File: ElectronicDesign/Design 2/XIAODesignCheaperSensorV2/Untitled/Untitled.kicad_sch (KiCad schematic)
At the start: 22 parts, among them U1 XIAO-ESP32-C3-SMD, U2 MPR121QR2, U3 QMI8658A_C3021082, U6 S2B-PH-K-S

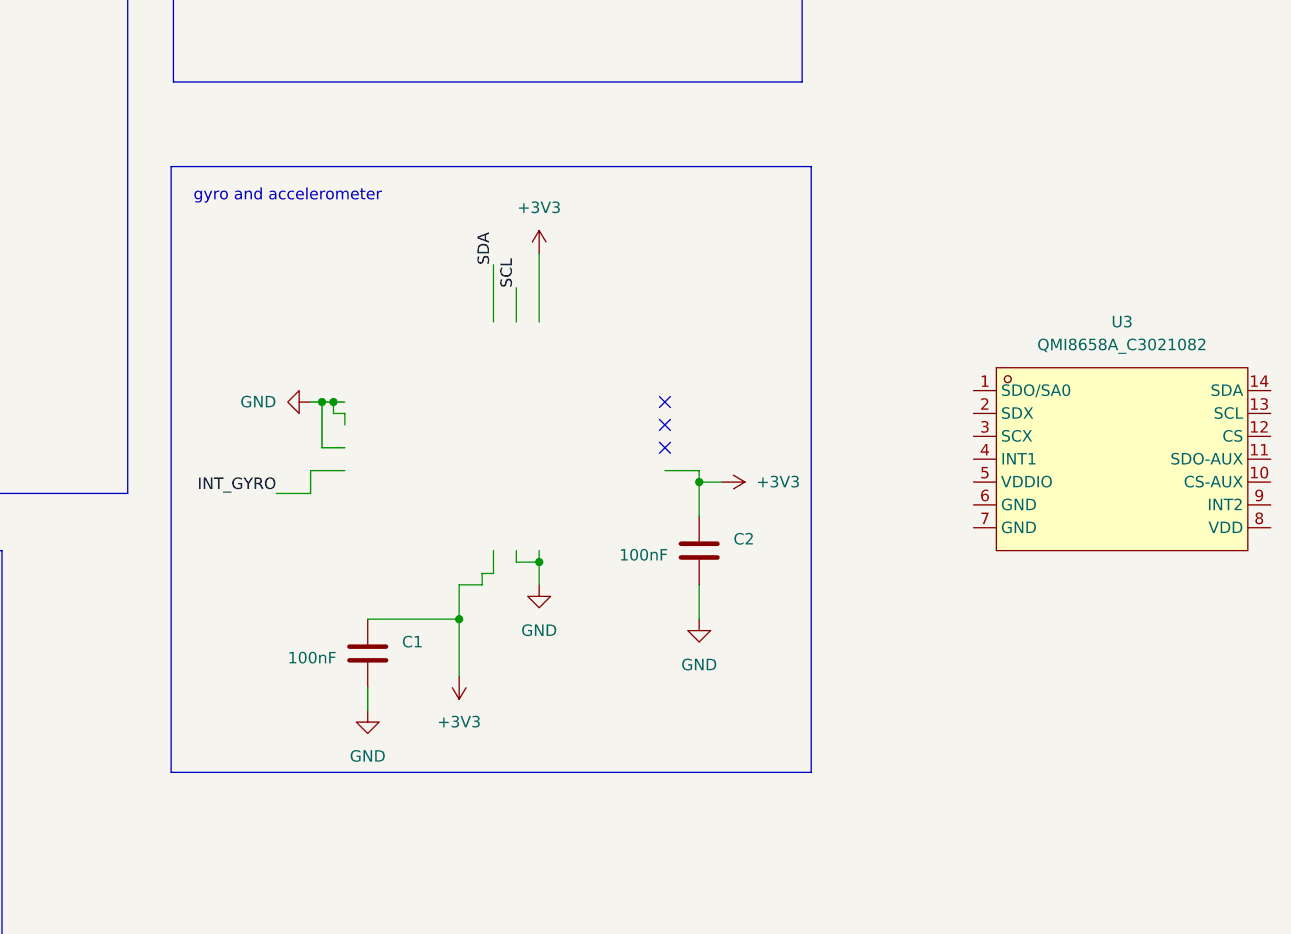
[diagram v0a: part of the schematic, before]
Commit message: Updated schematic with new component
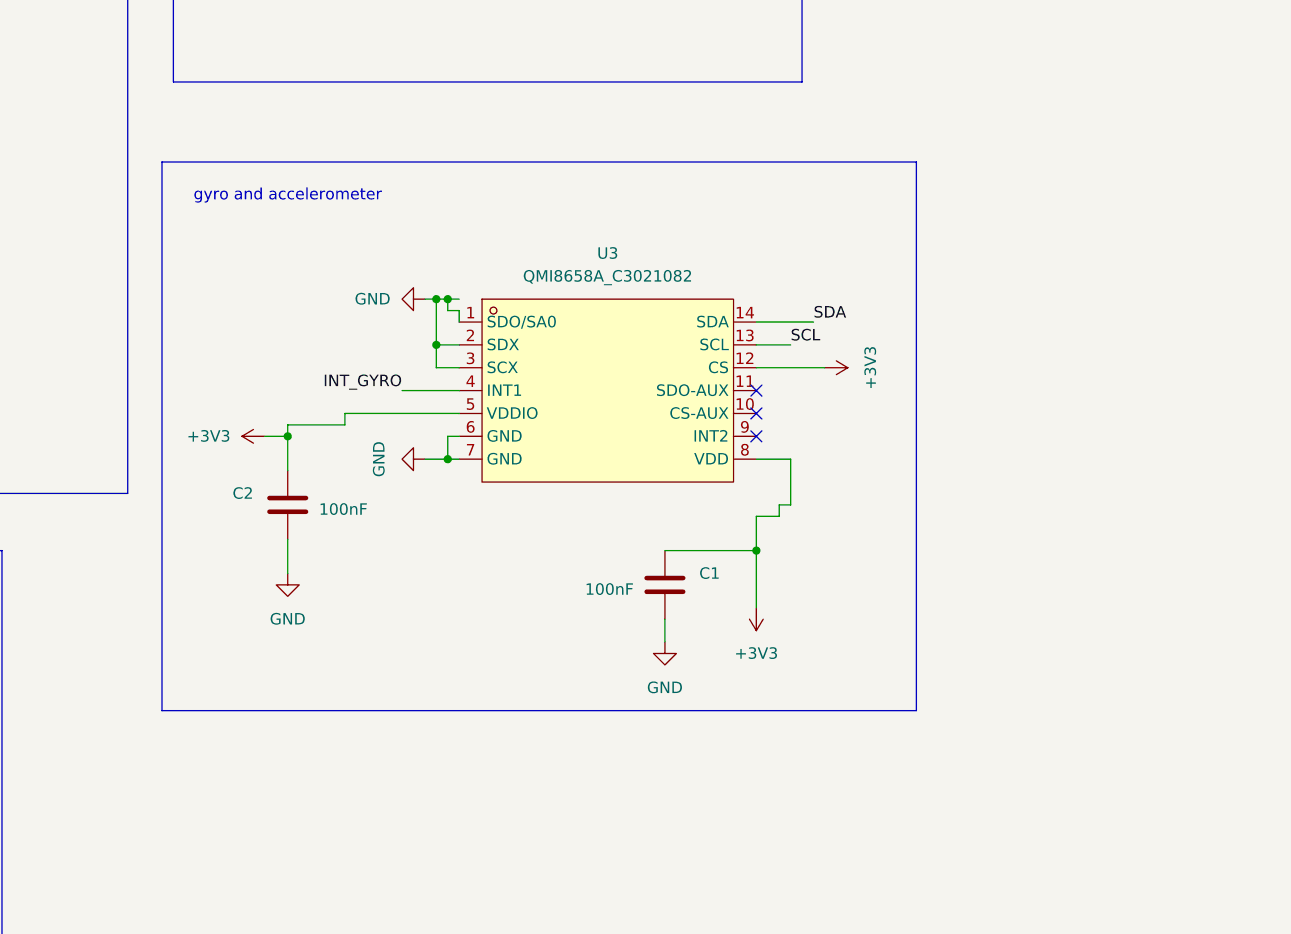
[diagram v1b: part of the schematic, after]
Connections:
- net +3V3: now also U3.12 (CS), U3.5 (VDDIO), U3.8 (VDD)
- net GND: now also U3.1 (SDO/SA0), U3.2 (SDX), U3.3 (SCX), U3.6 (GND), U3.7 (GND)
- net INT_GYRO: now also U3.4 (INT1)
- net SCL: now also U3.13 (SCL)
- net SDA: now also U3.14 (SDA)
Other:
- moved on the sheet: C1, C2, U3
